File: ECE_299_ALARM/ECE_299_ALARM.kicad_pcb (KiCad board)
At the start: 2 copper layers, 60 x 50 mm, 16 parts, among them SW1 SW_Push_Dual, SW2 SW_Push_Dual, SW3 SW_Push_Dual, SW4 SW_Push_Dual, U1 RDA5807M_Module, U2 RPi_Pico_TH, U3 LM386

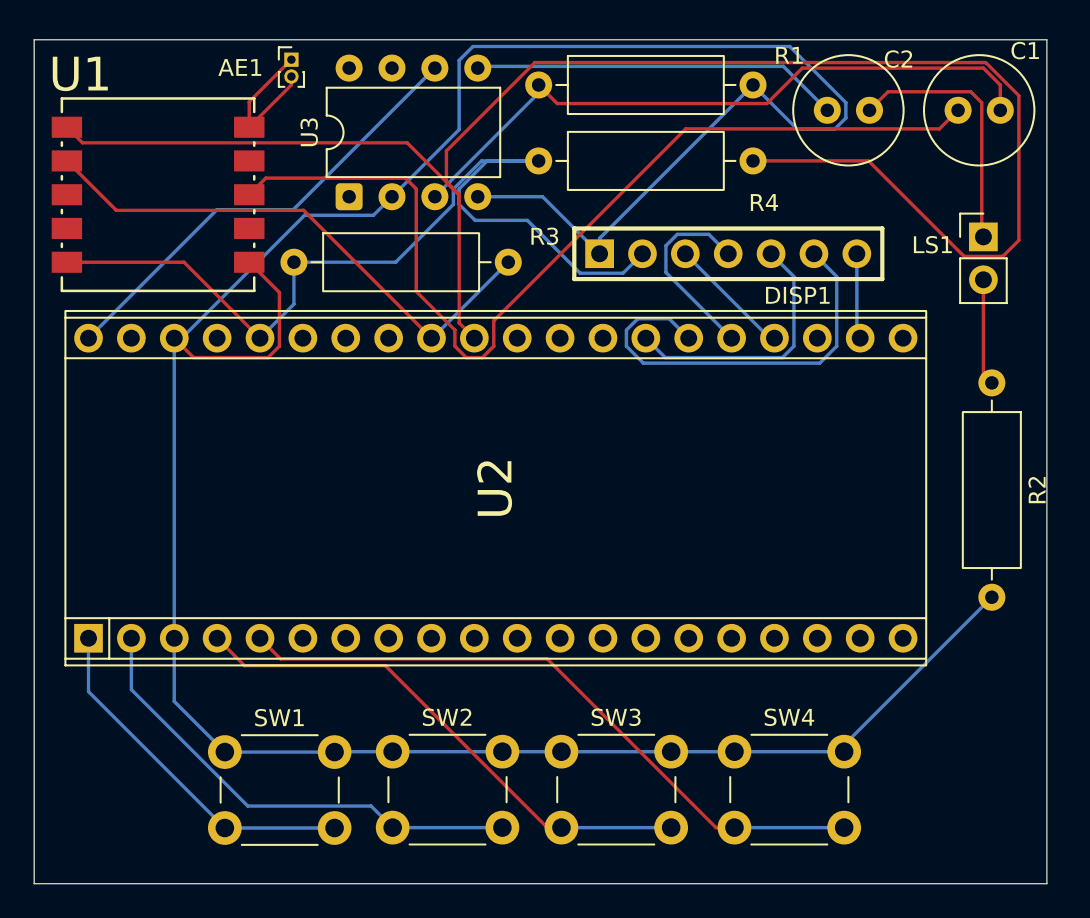
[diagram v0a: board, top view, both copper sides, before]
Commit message: error handling for radio and update pcb
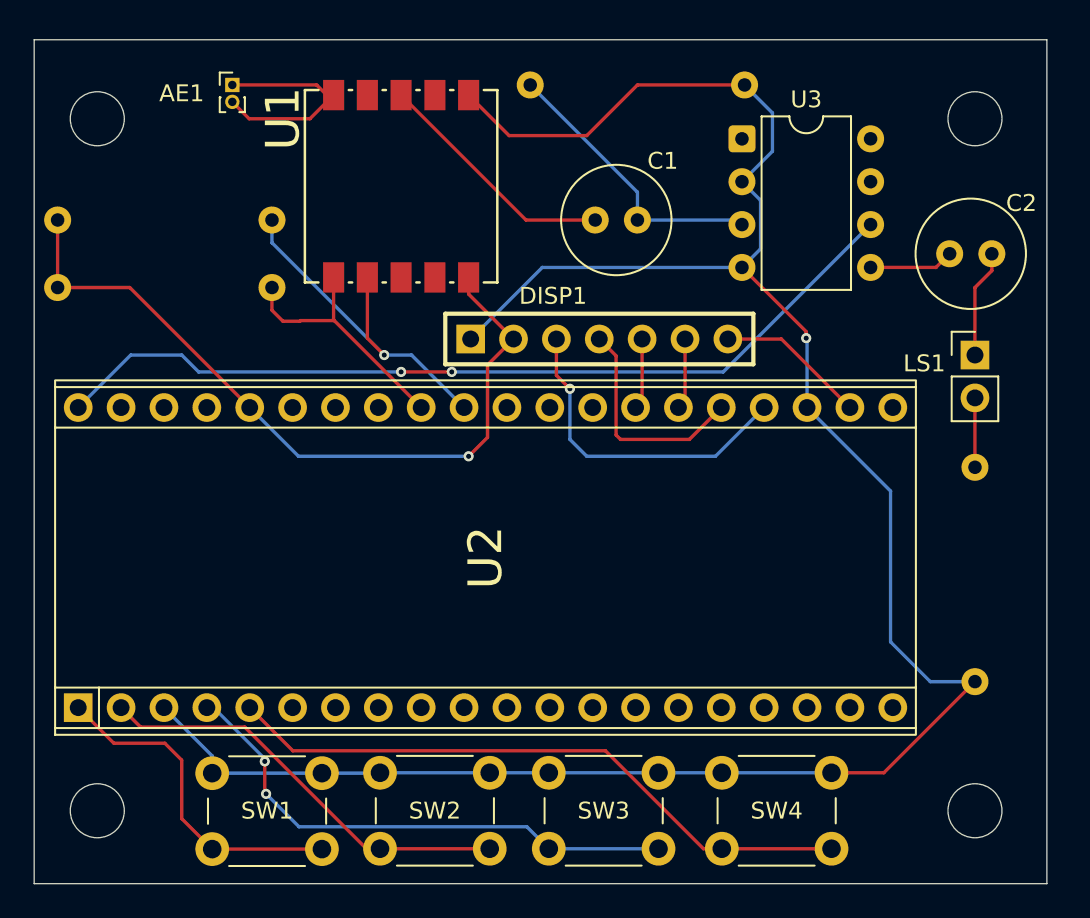
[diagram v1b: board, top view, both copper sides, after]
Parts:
- added REF**: MountingHole_3.2mm_M3, MountingHole:MountingHole_3.2mm_M3, F.Cu at (90.0, 115.0)
- added REF**: MountingHole_3.2mm_M3, MountingHole:MountingHole_3.2mm_M3, F.Cu at (142.0, 115.0)
- added REF**: MountingHole_3.2mm_M3, MountingHole:MountingHole_3.2mm_M3, F.Cu at (142.0, 74.0)
- added REF**: MountingHole_3.2mm_M3, MountingHole:MountingHole_3.2mm_M3, F.Cu at (90.0, 74.0)
- R1, R2, R3, R4: moved to B.Cu
- moved R4 28.7 mm to (87.7, 80.0)
- moved U3 23.5 mm to (128.2, 75.2), turned to 0 degrees
- moved C1 22.5 mm to (119.5, 80.0)
- moved U1 14.4 mm to (108.0, 78.0), turned to 90 degrees
- moved R3 14.1 mm to (87.7, 84.0)
- moved C2 11.2 mm to (140.5, 82.0)
- moved DISP1 9.16 mm to (102.0, 119.0)
- moved LS1 7.02 mm to (142.0, 88.0)
- moved R2 5.10 mm to (142.0, 94.7)
- moved U2 4.16 mm to (113.0, 100.0)
- moved AE1 3.81 mm to (98.0, 72.0)
- moved SW1 1.46 mm to (96.8, 112.8)
- moved SW2 1.46 mm to (106.8, 112.8)
- moved SW3 1.46 mm to (116.8, 112.8)
- moved SW4 1.46 mm to (127.0, 112.8)
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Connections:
- R3 pad 2: Net-(U1-SCLK) -> Net-(U1-SDIO)
- R4 pad 2: Net-(U1-SDIO) -> Net-(U1-SCLK)
- U2 pad 23: unconnected-(U2-GND-Pad23) -> GND
- U2 pad 31: Net-(U1-SDIO) -> Net-(U1-SCLK)
- U2 pad 32: Net-(U1-SCLK) -> Net-(U1-SDIO)
- U2 pad 38: GND -> unconnected-(U2-GND-Pad38)
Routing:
- net Net-(U1-SDIO): track 100.6 -> 15.2 mm
- net Net-(U1-LOUT): track 57.9 -> 14.6 mm
- net GND: track 168.8 -> 133.9 mm, vias 0 -> 1
- net +5V: track 27.1 -> 52.3 mm, vias 0 -> 2
- net Net-(U3-+): track 40.8 -> 16.9 mm
- net Net-(DISP1-DC): track 24.7 -> 4.22 mm
- net Net-(C2-Pad1): track 21.8 -> 5.02 mm
- net Net-(DISP1-SCLK): track 7.35 -> 19.4 mm, vias 0 -> 1
- net Net-(DISP1-RES): track 15.6 -> 4.22 mm
- net Net-(U1-SCLK): track 32.4 -> 21.8 mm, vias 0 -> 1
- net +3.3V: track 55.5 -> 45.3 mm, vias 0 -> 1
- net Net-(C2-Pad2): track 15.4 -> 6.41 mm
- net Net-(U1-FMIN): track 9.07 -> 13.2 mm
- net Net-(DISP1-CS): track 5.08 -> 8.91 mm
- net SW2: track 28.4 -> 25.3 mm
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
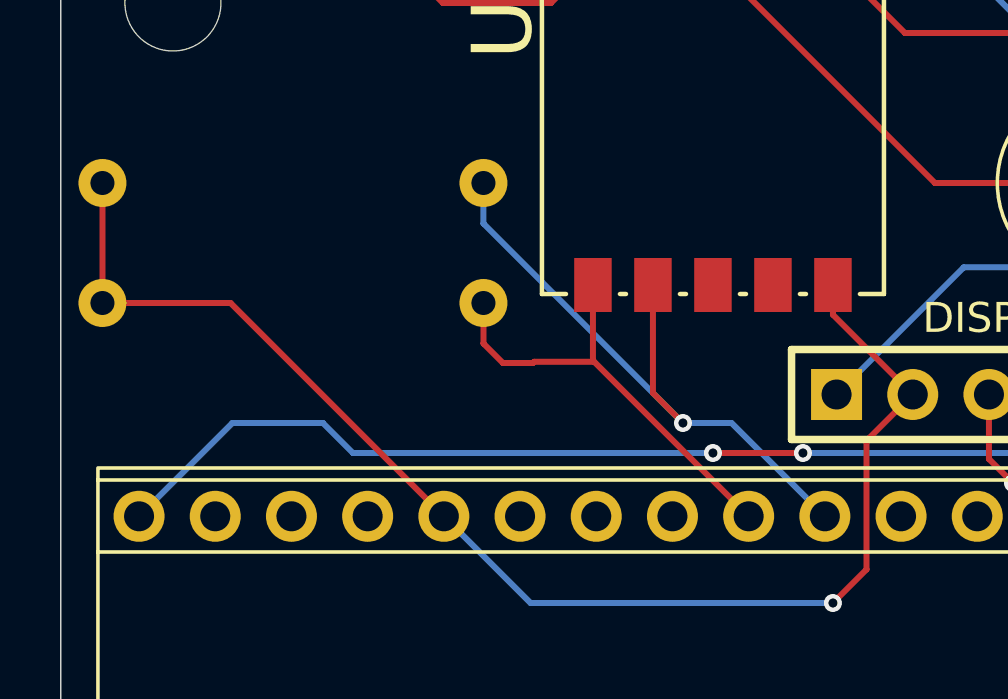
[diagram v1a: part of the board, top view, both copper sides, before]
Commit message: fix swapped SDA and SCL on radio module
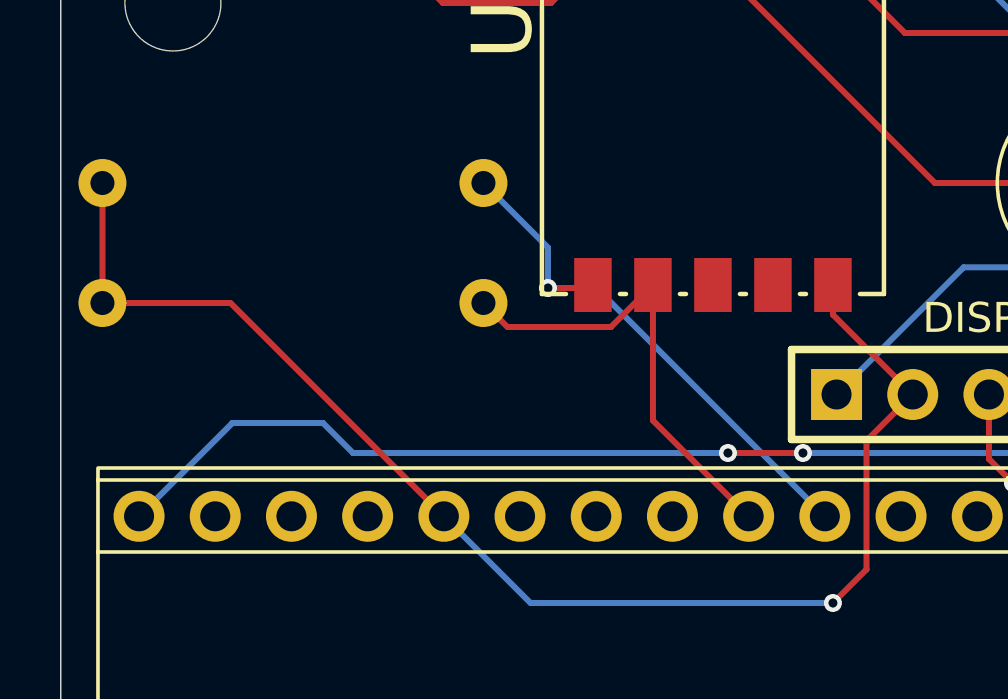
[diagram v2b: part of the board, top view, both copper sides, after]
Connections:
- R3 pad 2: Net-(U1-SDIO) -> Net-(U1-SCLK)
- R4 pad 2: Net-(U1-SCLK) -> Net-(U1-SDIO)
- U2 pad 31: Net-(U1-SCLK) -> Net-(U1-SDIO)
- U2 pad 32: Net-(U1-SDIO) -> Net-(U1-SCLK)
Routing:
- net Net-(U1-SCLK): track 21.8 -> 15.6 mm, vias 1 -> 0
- net Net-(U1-SDIO): track 15.2 -> 18.3 mm, vias 0 -> 1
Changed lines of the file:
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@@
 			)
 		)
-		(property "Datasheet" ""
+		(property "Datasheet" "~"
 			(at 0 0 0)
 			(layer "F.Fab")
@@
 			)
 		)
-		(property "Datasheet" ""
+		(property "Datasheet" "~"
 			(at 0 0 0)
 			(unlocked yes)
@@
 			)
 		)
-		(property "Datasheet" ""
+		(property "Datasheet" "~"
 			(at 0 0 0)
 			(layer "F.Fab")
@@
 			)
 		)
-		(property "Datasheet" ""
+		(property "Datasheet" "~"
 			(at 0 0 0)
 			(layer "F.Fab")
@@
 			)
 		)
-		(property "Datasheet" ""
+		(property "Datasheet" "~"
 			(at 0 0 0)
 			(unlocked yes)
@@
 			)
 		)
-		(property "Datasheet" ""
+		(property "Datasheet" "~"
 			(at 0 0 0)
 			(unlocked yes)
@@
 			)
 		)
-		(property "Datasheet" ""
+		(property "Datasheet" "~"
 			(at 0 0 0)
 			(layer "F.Fab")
@@
 			(layers "*.Cu" "*.Mask")
 			(remove_unused_layers no)
-			(net 14 "Net-(U1-SCLK)")
+			(net 15 "Net-(U1-SDIO)")
 			(pinfunction "GP26/ADC0")
 			(pintype "bidirectional")
@@
 			(layers "*.Cu" "*.Mask")
 			(remove_unused_layers no)
-			(net 15 "Net-(U1-SDIO)")
+			(net 14 "Net-(U1-SCLK)")
 			(pinfunction "GP27/ADC1")
 			(pintype "bidirectional")
@@
 			)
 		)
-		(property "Datasheet" ""
+		(property "Datasheet" "~"
 			(at 0 0 0)
 			(unlocked yes)
@@
 			)
 		)
-		(property "Datasheet" ""
+		(property "Datasheet" "~"
 			(at 0 0 0)
 			(layer "B.Fab")
@@
 			(layers "*.Cu" "*.Mask")
 			(remove_unused_layers no)
-			(net 15 "Net-(U1-SDIO)")
+			(net 14 "Net-(U1-SCLK)")
 			(pintype "passive")
 		)
@@
 			)
 		)
-		(property "Datasheet" ""
+		(property "Datasheet" "~"
 			(at 0 0 90)
 			(layer "B.Fab")
@@
 			)
 		)
-		(property "Datasheet" ""
+		(property "Datasheet" "~"
 			(at 0 0 0)
 			(layer "B.Fab")
@@
 			)
 		)
-		(property "Datasheet" ""
+		(property "Datasheet" "~"
 			(at 0 0 0)
 			(layer "B.Fab")
@@
 			(layers "*.Cu" "*.Mask")
 			(remove_unused_layers no)
-			(net 14 "Net-(U1-SCLK)")
+			(net 15 "Net-(U1-SDIO)")
 			(pintype "passive")
 		)
@@
 	)
 	(segment
-		(start 106 87)
-		(end 106 83.4)
+		(start 106 87.92)
+		(end 109.19 91.11)
 		(width 0.2)
 		(layer "F.Cu")
@@
 	)
 	(segment
-		(start 107 88)
-		(end 106 87)
+		(start 104.600001 84.799999)
+		(end 106 83.4)
 		(width 0.2)
 		(layer "F.Cu")
 		(net 14)
 	)
-	(via
-		(at 107 88)
-		(size 0.6)
-		(drill 0.3)
-		(layers "F.Cu" "B.Cu")
-		(net 14)
-	)
 	(segment
-		(start 100.35 81.35)
-		(end 100.35 80)
+		(start 106 83.4)
+		(end 106 87.92)
 		(width 0.2)
-		(layer "B.Cu")
-		(net 14)
-	)
-	(segment
-		(start 108.62 88)
-		(end 107 88)
-		(width 0.2)
-		(layer "B.Cu")
+		(layer "F.Cu")
 		(net 14)
 	)
 	(segment
-		(start 107 88)
-		(end 100.35 81.35)
+		(start 101.149999 84.799999)
+		(end 104.600001 84.799999)
 		(width 0.2)
-		(layer "B.Cu")
+		(layer "F.Cu")
 		(net 14)
 	)
 	(segment
-		(start 111.73 91.11)
-		(end 108.62 88)
+		(start 100.35 84)
+		(end 101.149999 84.799999)
 		(width 0.2)
-		(layer "B.Cu")
+		(layer "F.Cu")
 		(net 14)
 	)
 	(segment
-		(start 104.04 85.96)
-		(end 102.04 85.96)
+		(start 103.9 83.5)
+		(end 104 83.4)
 		(width 0.2)
 		(layer "F.Cu")
@@
 	)
 	(segment
-		(start 100.35 85.35)
-		(end 100.35 84)
+		(start 102.5 83.5)
+		(end 103.9 83.5)
 		(width 0.2)
 		(layer "F.Cu")
 		(net 15)
 	)
-	(segment
-		(start 104 85.92)
-		(end 104 83.4)
-		(width 0.2)
-		(layer "F.Cu")
+	(via
+		(at 102.5 83.5)
+		(size 0.6)
+		(drill 0.3)
+		(layers "F.Cu" "B.Cu")
 		(net 15)
 	)
 	(segment
-		(start 104.04 85.96)
-		(end 104 85.92)
+		(start 102.5 83.5)
+		(end 104.12 83.5)
 		(width 0.2)
-		(layer "F.Cu")
+		(layer "B.Cu")
 		(net 15)
 	)
 	(segment
-		(start 109.19 91.11)
-		(end 104.04 85.96)
+		(start 110.221 89.601)
+		(end 111.73 91.11)
 		(width 0.2)
-		(layer "F.Cu")
+		(layer "B.Cu")
 		(net 15)
 	)
 	(segment
-		(start 102.04 85.96)
-		(end 102 86)
+		(start 102.5 82.15)
+		(end 100.35 80)
 		(width 0.2)
-		(layer "F.Cu")
+		(layer "B.Cu")
 		(net 15)
 	)
 	(segment
-		(start 102 86)
-		(end 101 86)
+		(start 102.5 83.5)
+		(end 102.5 82.15)
 		(width 0.2)
-		(layer "F.Cu")
+		(layer "B.Cu")
 		(net 15)
 	)
 	(segment
-		(start 101 86)
-		(end 100.35 85.35)
+		(start 104.12 83.5)
+		(end 110.221 89.601)
 		(width 0.2)
-		(layer "F.Cu")
+		(layer "B.Cu")
 		(net 15)
 	)
@@
 	)
 	(segment
-		(start 108 89)
+		(start 108.5 89)
 		(end 111 89)
 		(width 0.2)
@@
 	)
 	(via
-		(at 108 89)
+		(at 108.5 89)
 		(size 0.6)
 		(drill 0.3)
@@
 	(segment
 		(start 91.98 88)
+		(end 88.87 91.11)
+		(width 0.2)
+		(layer "B.Cu")
+		(net 26)
+	)
+	(segment
+		(start 96 89)
 		(end 95 88)
 		(width 0.2)
@@
 	)
 	(segment
-		(start 95 88)
+		(start 108.5 89)
 		(end 96 89)
 		(width 0.2)
@@
 	)
 	(segment
-		(start 96 89)
-		(end 108 89)
+		(start 95 88)
+		(end 91.98 88)
 		(width 0.2)
 		(layer "B.Cu")
@@
 		(width 0.2)
 		(layer "B.Cu")
-		(net 26)
-	)
-	(segment
-		(start 88.87 91.11)
-		(end 91.98 88)
-		(width 0.2)
-		(layer "B.Cu")

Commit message: i just wasted an hour making better routing
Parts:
- R1: value 10k -> 1k; moved to F.Cu
- R3, R4: moved to F.Cu
- moved R1 12.9 mm to (128.5, 71.5), turned to 180 degrees
- moved R3 0.61 mm to (88.0, 83.5)
- moved R4 0.61 mm to (88.0, 79.5)
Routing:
- net +3.3V: track 45.3 -> 39.3 mm, vias 1 -> 2
- net Net-(DISP1-SCLK): track 19.4 -> 14.0 mm
- net +5V: track 52.3 -> 57.6 mm, vias 2 -> 4
- net Net-(DISP1-SDA): track 13.2 -> 9.61 mm
- net Net-(U1-LOUT): track 14.6 -> 18.1 mm, vias 0 -> 1
- net GND: track 133.9 -> 132.6 mm
- net Net-(U1-SDIO): track 18.3 -> 19.3 mm

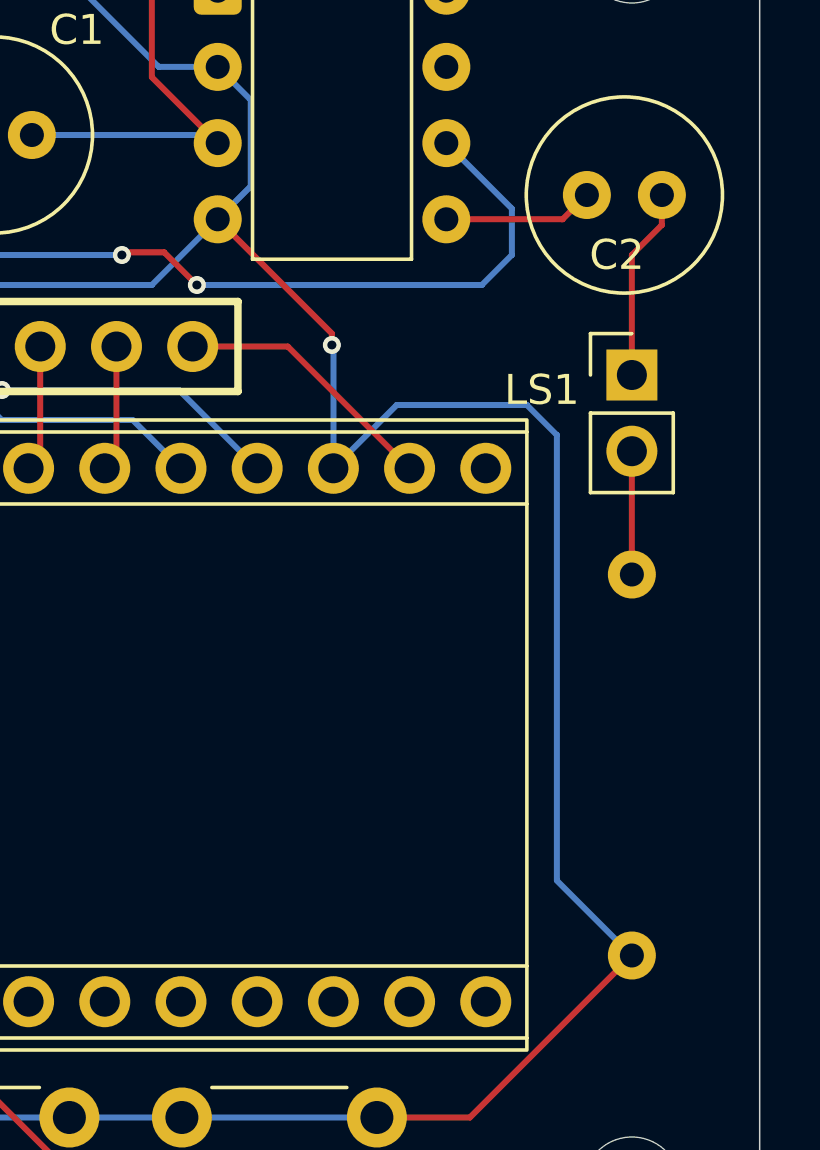
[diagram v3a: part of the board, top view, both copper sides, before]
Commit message: add high current path, 1mm is probably excessive
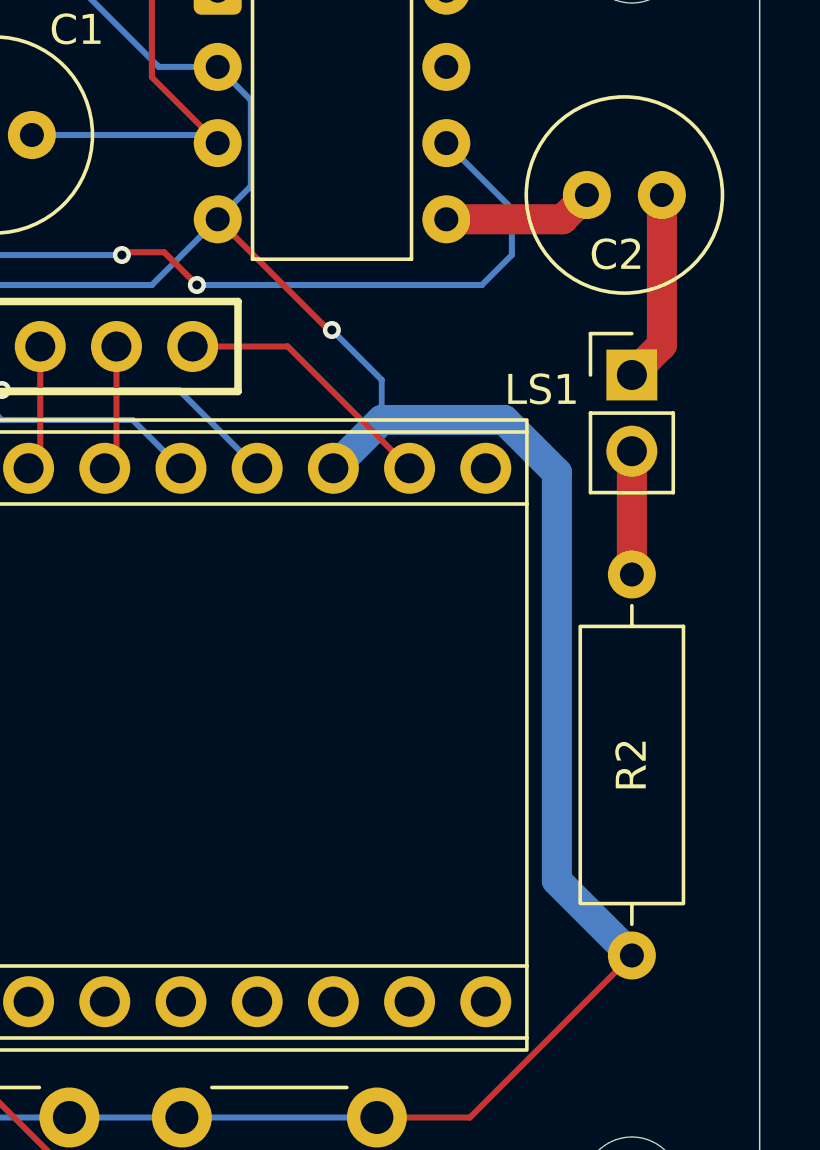
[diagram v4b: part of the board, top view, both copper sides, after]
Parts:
- R2: moved to F.Cu
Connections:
- net Net-(DISP1-CS) renamed CS
- net Net-(DISP1-DC) renamed DC
- net Net-(DISP1-RES) renamed RES
- net Net-(DISP1-SCLK) renamed SCLK
- net Net-(DISP1-SDA) renamed SDA
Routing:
- net GND: track 132.6 -> 130.6 mm
